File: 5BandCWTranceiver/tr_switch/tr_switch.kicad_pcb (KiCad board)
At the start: 2 copper layers, 44 x 49.5 mm, 42 parts, among them J1 Conn_01x02, J10 Conn_01x02_Male, J11 Conn_01x02_Male, J12 Conn_01x02_Male, J2 Conn_01x02, J3 Conn_01x02, J4 Conn_Coaxial, J5 Conn_01x02, J6 Conn_Coaxial, J7 Conn_Coaxial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

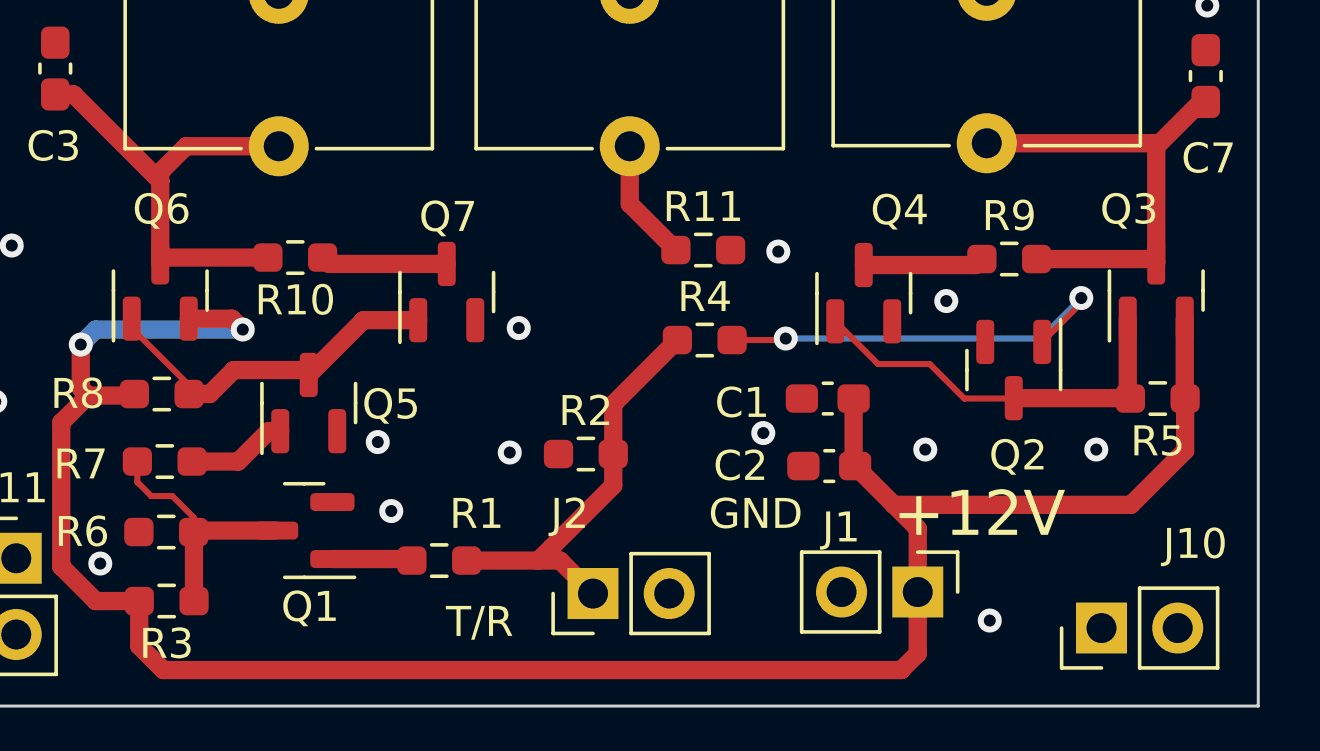
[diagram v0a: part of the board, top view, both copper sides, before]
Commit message: TRSwitch - added resistor
Added 10K resistors to reduce current in bias switching
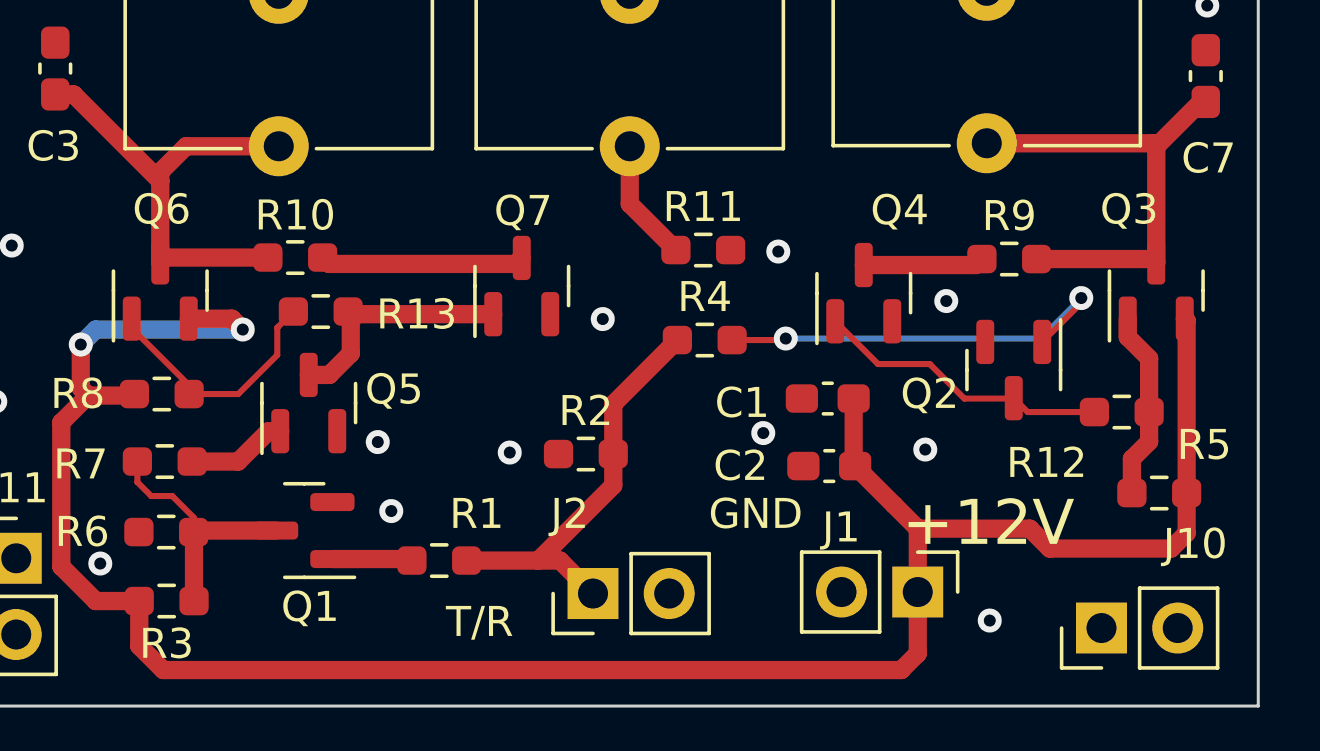
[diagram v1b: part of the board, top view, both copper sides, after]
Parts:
- added R12: 10K, Resistor_SMD:R_0603_1608Metric_Pad0.98x0.95mm_HandSolder, F.Cu at (118.7, 101.0)
- added R13: 10K, Resistor_SMD:R_0603_1608Metric_Pad0.98x0.95mm_HandSolder, F.Cu at (92.0, 97.6)
- moved R5 3.15 mm to (120.0, 103.7)
- moved Q7 2.51 mm to (98.7, 96.8)
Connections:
- Q3 pad 1: Net-(Q2-Pad3) -> Net-(Q3-Pad1)
- Q6 pad 1: Net-(Q5-Pad3) -> Net-(Q6-Pad1)
- R5 pad 2: Net-(Q2-Pad3) -> Net-(Q3-Pad1)
- R8 pad 2: Net-(Q5-Pad3) -> Net-(Q6-Pad1)
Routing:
- net Net-(Q6-Pad1): track 0.00 -> 8.45 mm
- net Net-(Q3-Pad1): track 0.00 -> 6.35 mm
- net Net-(Q5-Pad3): track 12.1 -> 7.88 mm
- net Net-(Q2-Pad3): track 13.6 -> 9.90 mm
- net Net-(Q7-Pad3): track 4.23 -> 6.81 mm
- net /VDD12: track 72.3 -> 74.1 mm
- net GND: vias 28 -> 27
